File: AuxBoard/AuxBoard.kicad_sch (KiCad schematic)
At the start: 15 parts, among them J1 ATX-24, J2 RPI4B, J3 USB_C_Receptacle_USB2.0, J4 MatrixASupply, J5 MatrixBSupply, J6 BigLEDSupply, SW1 SW_DPST, U1 74125

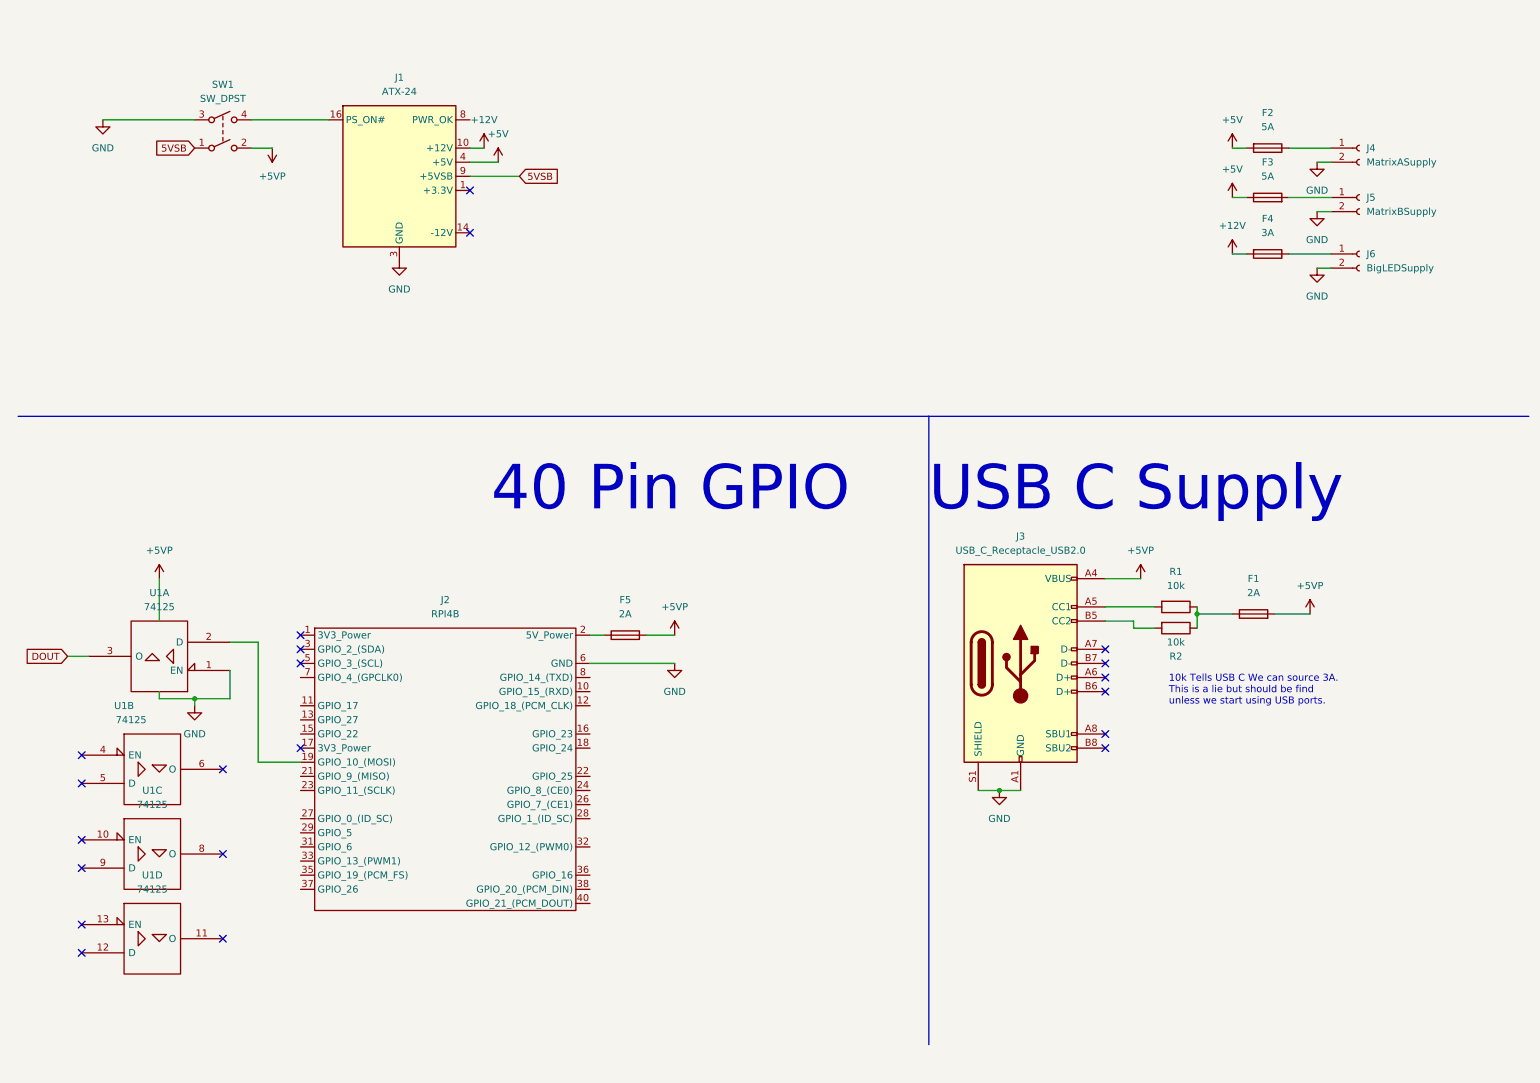
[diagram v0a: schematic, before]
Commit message: Added headers to handle comms with Matrices and Big LED
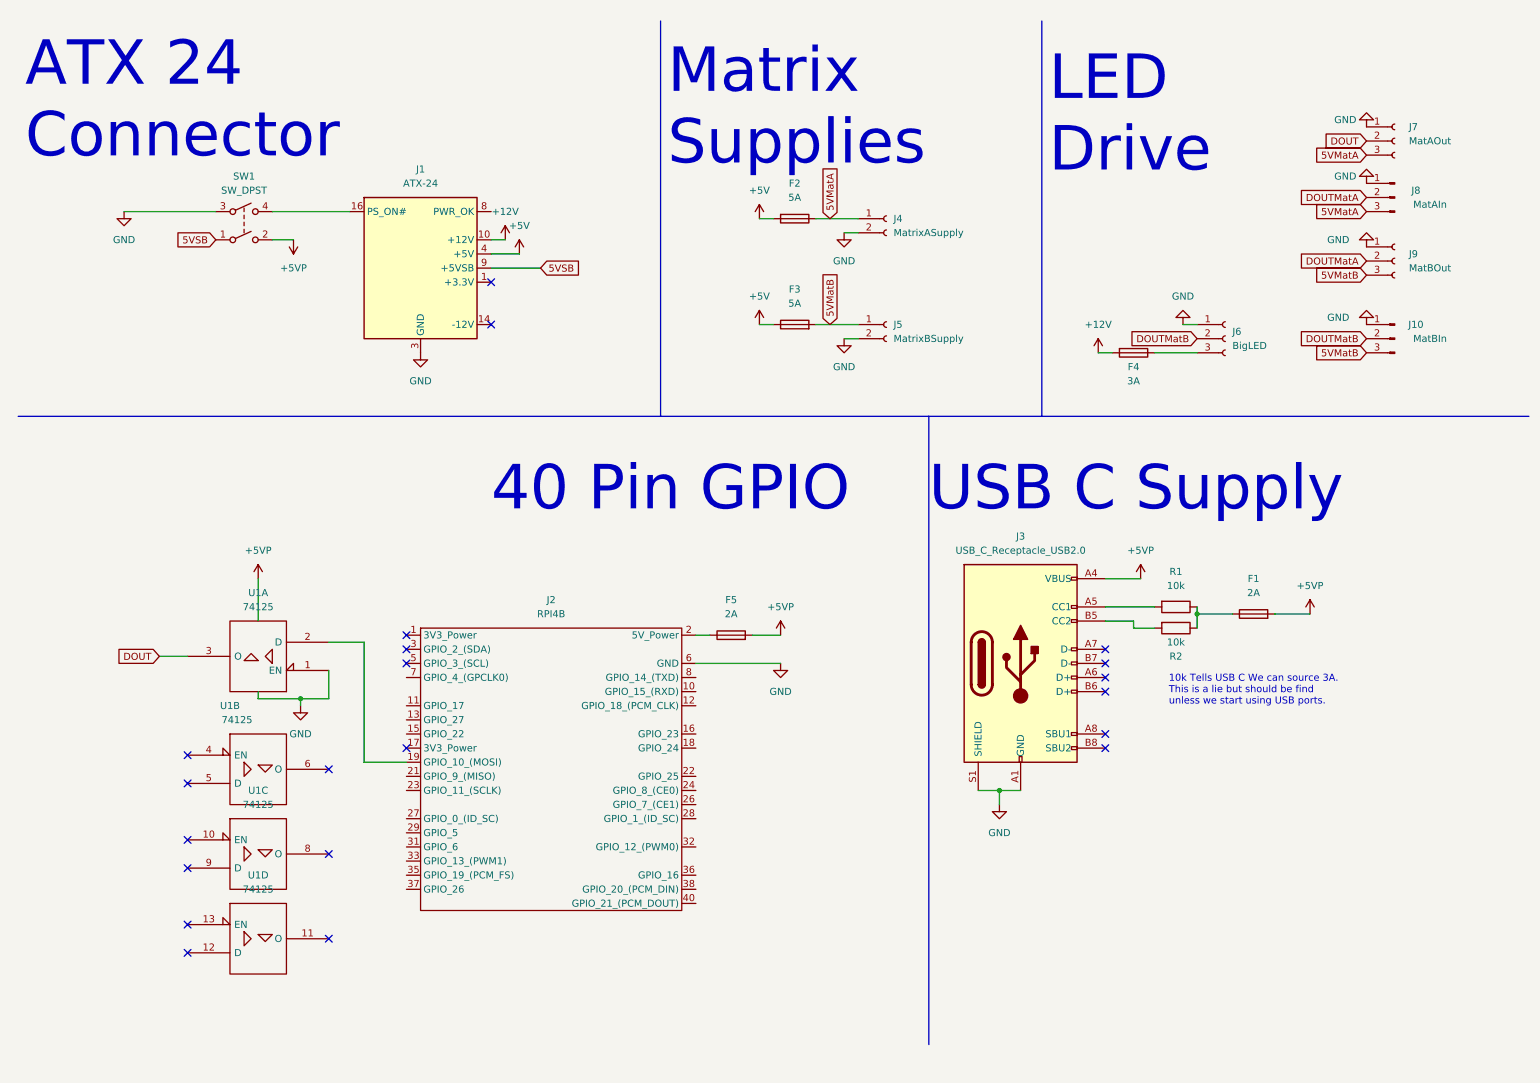
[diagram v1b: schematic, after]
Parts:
- removed J6: BigLEDSupply, symbol Connector:Conn_01x02_Female
- added J10: MatBIn, Connector_PinSocket_2.54mm:PinSocket_1x03_P2.54mm_Vertical, symbol Connector:Conn_01x03_Male
- added J6: BigLED, Connector_PinSocket_2.54mm:PinSocket_1x03_P2.54mm_Vertical, symbol Connector:Conn_01x03_Female
- added J7: MatAOut, Connector_PinSocket_2.54mm:PinSocket_1x03_P2.54mm_Vertical, symbol Connector:Conn_01x03_Female
- added J8: MatAIn, Connector_PinSocket_2.54mm:PinSocket_1x03_P2.54mm_Vertical, symbol Connector:Conn_01x03_Male
- added J9: MatBOut, Connector_PinSocket_2.54mm:PinSocket_1x03_P2.54mm_Vertical, symbol Connector:Conn_01x03_Female
- U1: footprint (none) -> Package_DIP:DIP-14_W7.62mm_LongPads
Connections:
- net +5VP: now also J10.1 (Pin_1), J6.1 (Pin_1), J7.1 (Pin_1), J8.1 (Pin_1), J9.1 (Pin_1)
- net DOUT: now also J7.2 (Pin_2)
- net 5VMatB: now reaches F3.2, J5.1 (Pin_1)
- net 5VMatB: now also J10.3 (Pin_3), J9.3 (Pin_3)
- net 5VMatA: now reaches F2.1, J4.1 (Pin_1)
- net 5VMatA: now also J7.3 (Pin_3), J8.3 (Pin_3)
- net at F4.1: now also J6.3 (Pin_3)
- new net DOUTMatA: J8.2 (Pin_2), J9.2 (Pin_2)
- new net DOUTMatB: J10.2 (Pin_2), J6.2 (Pin_2)
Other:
- note added: "ATX 24 Connector"
- note added: "LED Drive"
- note added: "Matrix Supplies"
- moved on the sheet: F2, F3, F4, F5, J1, J2, J4, J5, SW1, U1A, U1B, U1C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

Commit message: Power Distro Changes
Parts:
- J2: footprint Connector_PinSocket_2.54mm:PinSocket_2x19_P2.54mm_Vertical_SMD -> Connector_PinSocket_2.54mm:PinSocket_2x20_P2.54mm_Vertical_SMD
- J4, J5: footprint (none) -> Connector_PinSocket_2.54mm:PinSocket_1x02_P2.54mm_Vertical
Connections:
- net 5V_Power is gone; now on an unnamed net: J2.4 (5V_Power)
- net +5VP: no longer J1.15 (GND), J1.17 (GND), J1.18 (GND), J1.19 (GND), J1.24 (GND), J1.3 (GND), J1.5 (GND), J1.7 (GND), J10.1 (Pin_1), J2.14 (GND), J2.20 (GND), J2.25 (GND), J2.30 (GND), J2.34 (GND), J2.39 (GND), J2.6 (GND), J2.9 (GND), J3.A1 (GND), J3.A12 (GND), J3.B1 (GND), J3.B12 (GND), J3.S1 (SHIELD), J4.2 (Pin_2), J5.2 (Pin_2), J6.1 (Pin_1), J7.1 (Pin_1), J8.1 (Pin_1), J9.1 (Pin_1), SW1.3, U1.1 (EN), U1.7 (GND), U1.7 (GND), U1.7 (GND), U1.7 (GND)
- net +3.3V: now reaches J1.1 (+3.3V), J1.12 (+3.3V), J1.13 (+3.3V), J1.2 (+3.3V)
- new net GND: J1.15 (GND), J1.17 (GND), J1.18 (GND), J1.19 (GND), J1.24 (GND), J1.3 (GND), J1.5 (GND), J1.7 (GND), J10.1 (Pin_1), J2.14 (GND), J2.20 (GND), J2.25 (GND), J2.30 (GND), J2.34 (GND), J2.39 (GND), J2.6 (GND), J2.9 (GND), J3.A1 (GND), J3.A12 (GND), J3.B1 (GND), J3.B12 (GND), J4.2 (Pin_2), J5.2 (Pin_2), J6.1 (Pin_1), J7.1 (Pin_1), J8.1 (Pin_1), J9.1 (Pin_1), SW1.3, U1.1 (EN), U1.7 (GND), U1.7 (GND), U1.7 (GND), U1.7 (GND)
- no-connect marks 21 -> 47
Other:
- moved on the sheet: F5, U1A, U1B, U1C, U1D

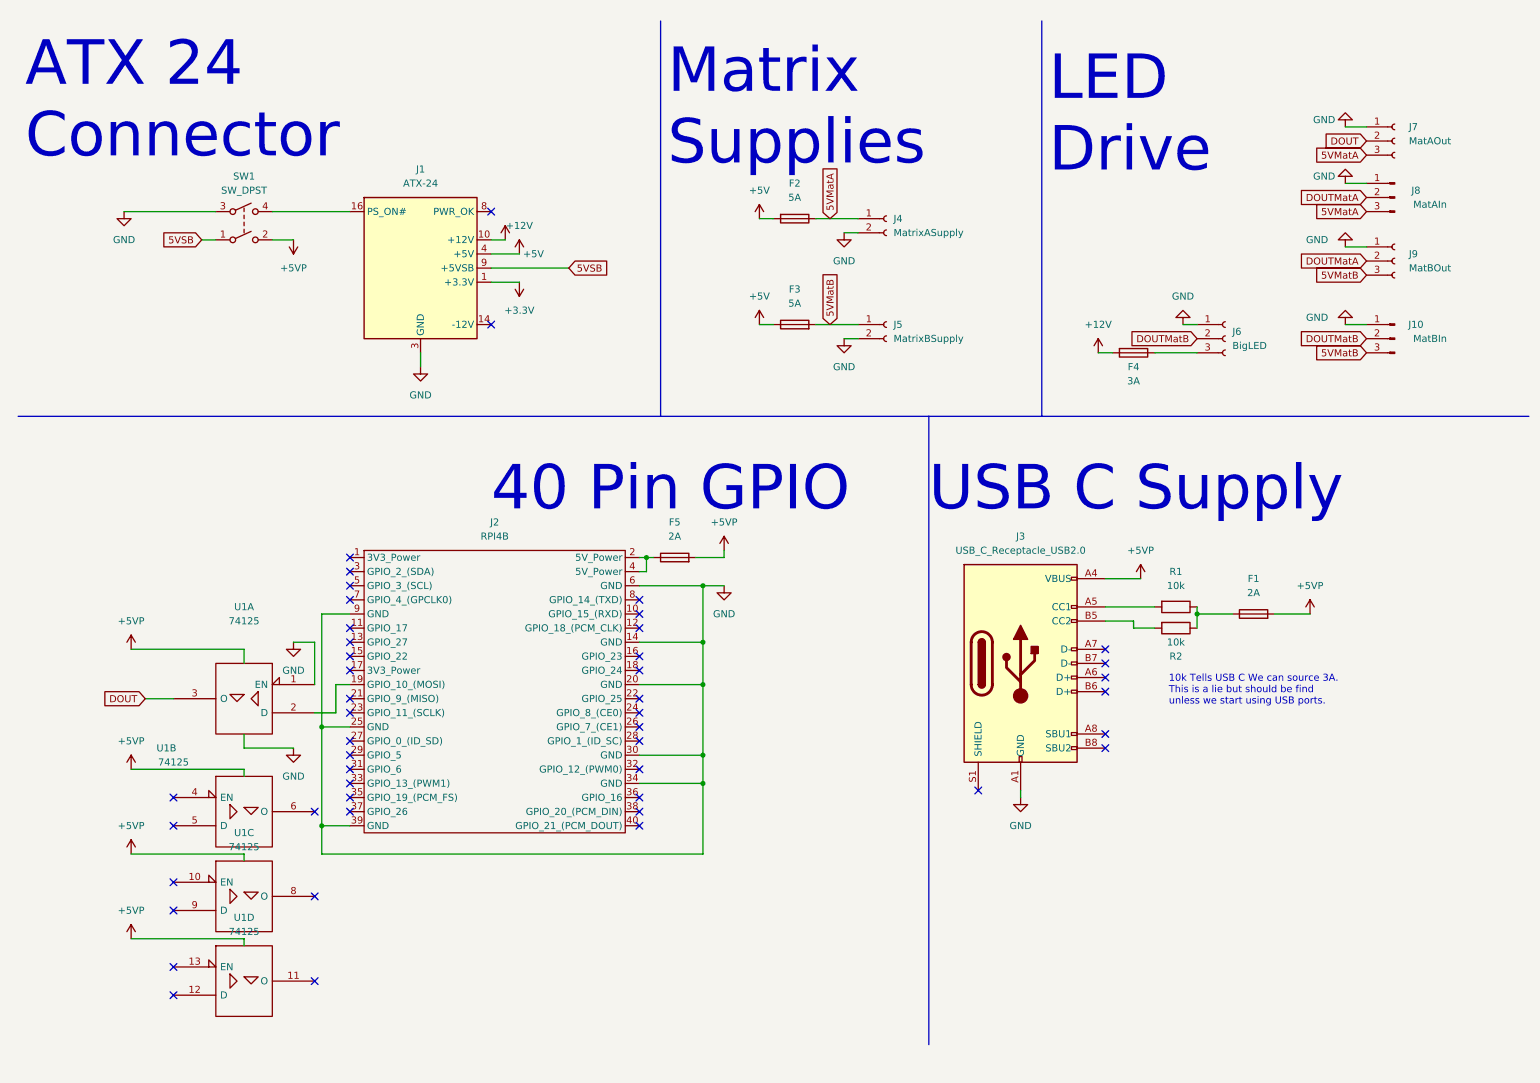
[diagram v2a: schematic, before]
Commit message: Added seccond GPIO
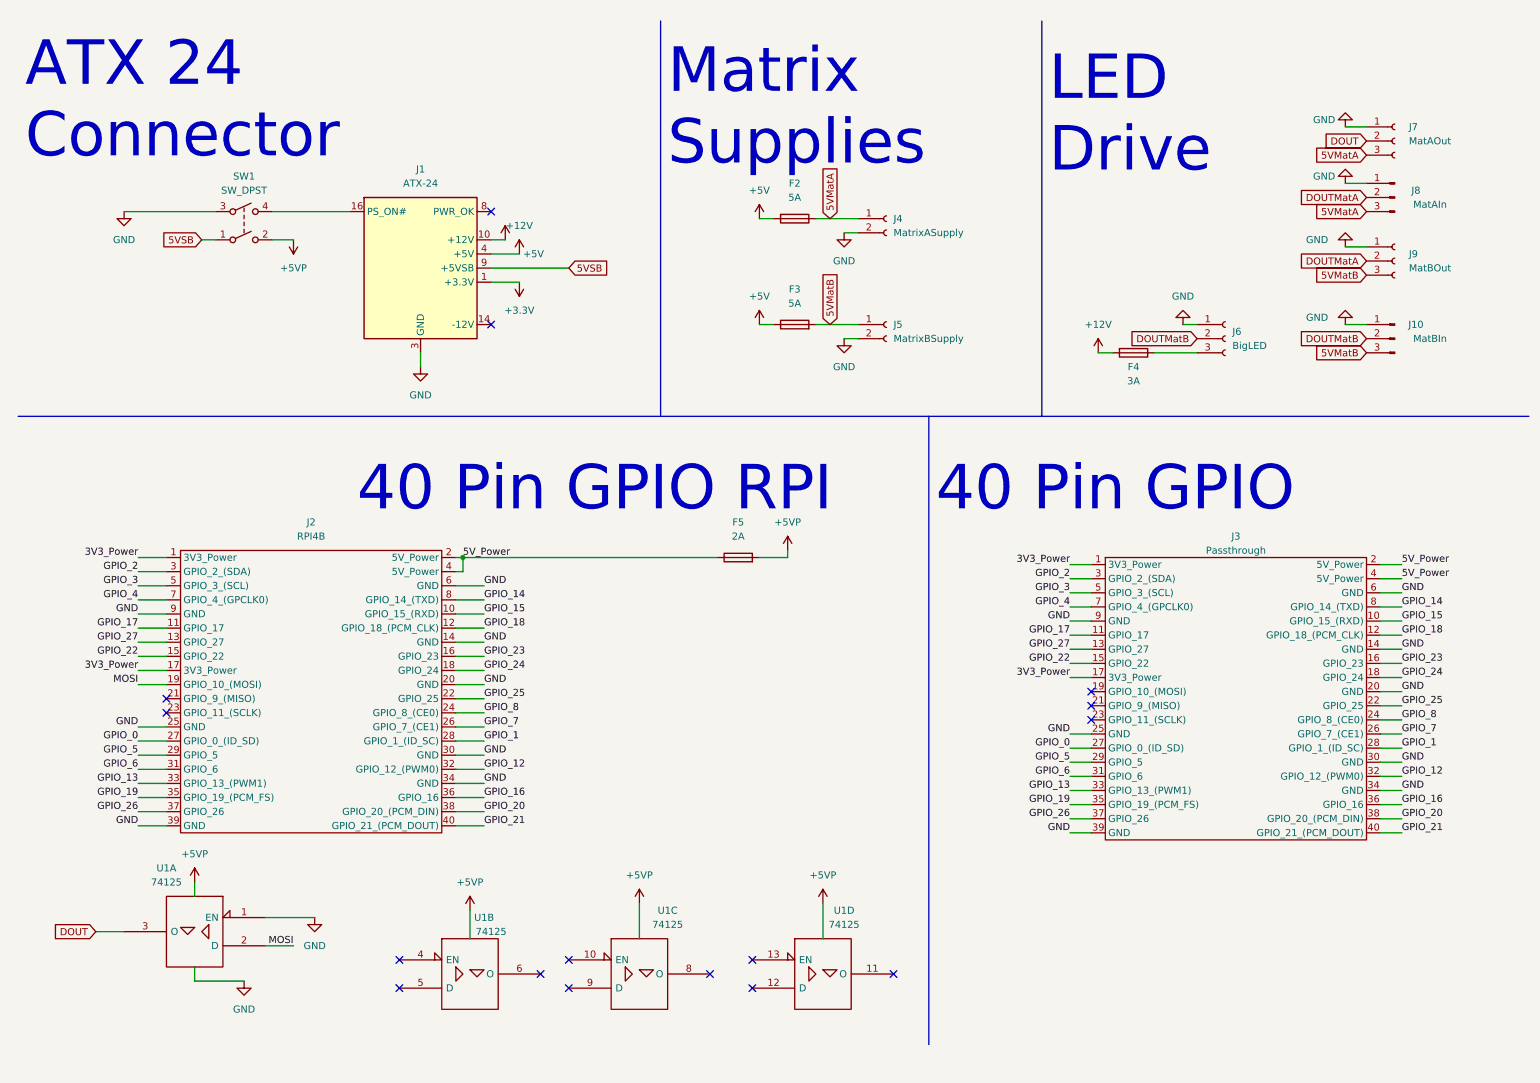
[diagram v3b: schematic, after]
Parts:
- removed F1: 2A, symbol Device:Fuse
- removed J3: USB_C_Receptacle_USB2.0, symbol Connector:USB_C_Receptacle_USB2.0
- removed R1, R2: 10k, symbol Device:R
- added J3: Passthrough, Connector_PinSocket_2.54mm:PinSocket_2x20_P2.54mm_FLIPED_Vertical_SMD, symbol Tom's Parts:RPI4B
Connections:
- net GND: now also J3.14 (GND), J3.20 (GND), J3.25 (GND), J3.30 (GND), J3.34 (GND), J3.39 (GND), J3.6 (GND), J3.9 (GND)
- net 3V3_Power: now reaches J2.1 (3V3_Power)
- net 3V3_Power: now also J2.17 (3V3_Power), J3.1 (3V3_Power), J3.17 (3V3_Power)
- net GPIO_15: now reaches J2.10 (GPIO_15_(RXD))
- net GPIO_15: now also J3.10 (GPIO_15_(RXD))
- net GPIO_17: now reaches J2.11 (GPIO_17)
- net GPIO_17: now also J3.11 (GPIO_17)
- net GPIO_18: now reaches J2.12 (GPIO_18_(PCM_CLK))
- net GPIO_18: now also J3.12 (GPIO_18_(PCM_CLK))
- net GPIO_27: now reaches J2.13 (GPIO_27)
- net GPIO_27: now also J3.13 (GPIO_27)
- net GPIO_22: now reaches J2.15 (GPIO_22)
- net GPIO_22: now also J3.15 (GPIO_22)
- net GPIO_23: now reaches J2.16 (GPIO_23)
- net GPIO_23: now also J3.16 (GPIO_23)
- net GPIO_24: now reaches J2.18 (GPIO_24)
- net GPIO_24: now also J3.18 (GPIO_24)
- net MOSI: now reaches J2.19 (GPIO_10_(MOSI)), U1.2 (D)
- net 5V_Power: now reaches F5.1, J2.2 (5V_Power), J2.4 (5V_Power)
- net 5V_Power: now also J3.2 (5V_Power), J3.4 (5V_Power)
- net GPIO_25: now reaches J2.22 (GPIO_25)
- net GPIO_25: now also J3.22 (GPIO_25)
- net GPIO_8: now reaches J2.24 (GPIO_8_(CE0))
- net GPIO_8: now also J3.24 (GPIO_8_(CE0))
- net GPIO_7: now reaches J2.26 (GPIO_7_(CE1))
- net GPIO_7: now also J3.26 (GPIO_7_(CE1))
- net GPIO_0: now reaches J2.27 (GPIO_0_(ID_SD))
- net GPIO_0: now also J3.27 (GPIO_0_(ID_SD))
- net GPIO_1: now reaches J2.28 (GPIO_1_(ID_SC))
- net GPIO_1: now also J3.28 (GPIO_1_(ID_SC))
- net GPIO_5: now reaches J2.29 (GPIO_5)
- net GPIO_5: now also J3.29 (GPIO_5)
- net GPIO_2: now reaches J2.3 (GPIO_2_(SDA))
- net GPIO_2: now also J3.3 (GPIO_2_(SDA))
- net GPIO_6: now reaches J2.31 (GPIO_6)
- net GPIO_6: now also J3.31 (GPIO_6)
- net GPIO_12: now reaches J2.32 (GPIO_12_(PWM0))
- net GPIO_12: now also J3.32 (GPIO_12_(PWM0))
- net GPIO_13: now reaches J2.33 (GPIO_13_(PWM1))
- net GPIO_13: now also J3.33 (GPIO_13_(PWM1))
- net GPIO_19: now reaches J2.35 (GPIO_19_(PCM_FS))
- net GPIO_19: now also J3.35 (GPIO_19_(PCM_FS))
- net GPIO_16: now reaches J2.36 (GPIO_16)
- net GPIO_16: now also J3.36 (GPIO_16)
- net GPIO_26: now reaches J2.37 (GPIO_26)
- net GPIO_26: now also J3.37 (GPIO_26)
- net GPIO_20: now reaches J2.38 (GPIO_20_(PCM_DIN))
- net GPIO_20: now also J3.38 (GPIO_20_(PCM_DIN))
- net GPIO_21: now reaches J2.40 (GPIO_21_(PCM_DOUT))
- net GPIO_21: now also J3.40 (GPIO_21_(PCM_DOUT))
- net GPIO_3: now reaches J2.5 (GPIO_3_(SCL))
- net GPIO_3: now also J3.5 (GPIO_3_(SCL))
- net GPIO_4: now reaches J2.7 (GPIO_4_(GPCLK0))
- net GPIO_4: now also J3.7 (GPIO_4_(GPCLK0))
- net GPIO_14: now reaches J2.8 (GPIO_14_(TXD))
- net GPIO_14: now also J3.8 (GPIO_14_(TXD))
- no-connect marks 47 -> 16
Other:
- note added: "40 Pin GPIO RPI"
- note removed: "10k Tells USB C We can source 3A. This is a lie but should be find unless we start using USB ports."
- note removed: "USB C Supply"
- title: (none) -> Auxillary Board for SynaesthetiQ
- moved on the sheet: F5, J2, U1A, U1B, U1C, U1D
